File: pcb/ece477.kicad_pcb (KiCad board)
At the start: 2 copper layers, 44 x 40 mm, 21 parts, among them J1 USB_B, SW1 SW_DIP_x01, U1 ESP32-WROOM-32, U2 FT232RL-REEL, U3 LM3671, U4 ADA254, U5 ADA751

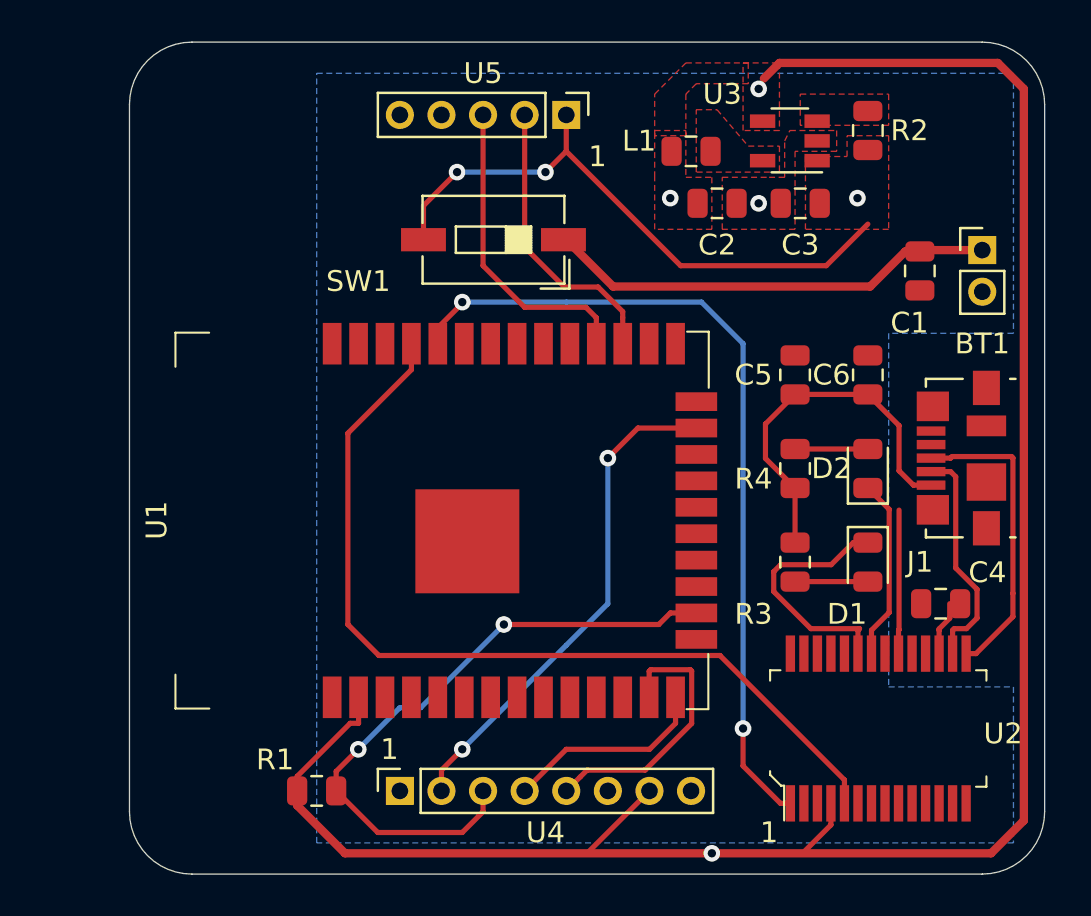
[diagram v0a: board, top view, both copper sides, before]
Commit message: connected to ground plate
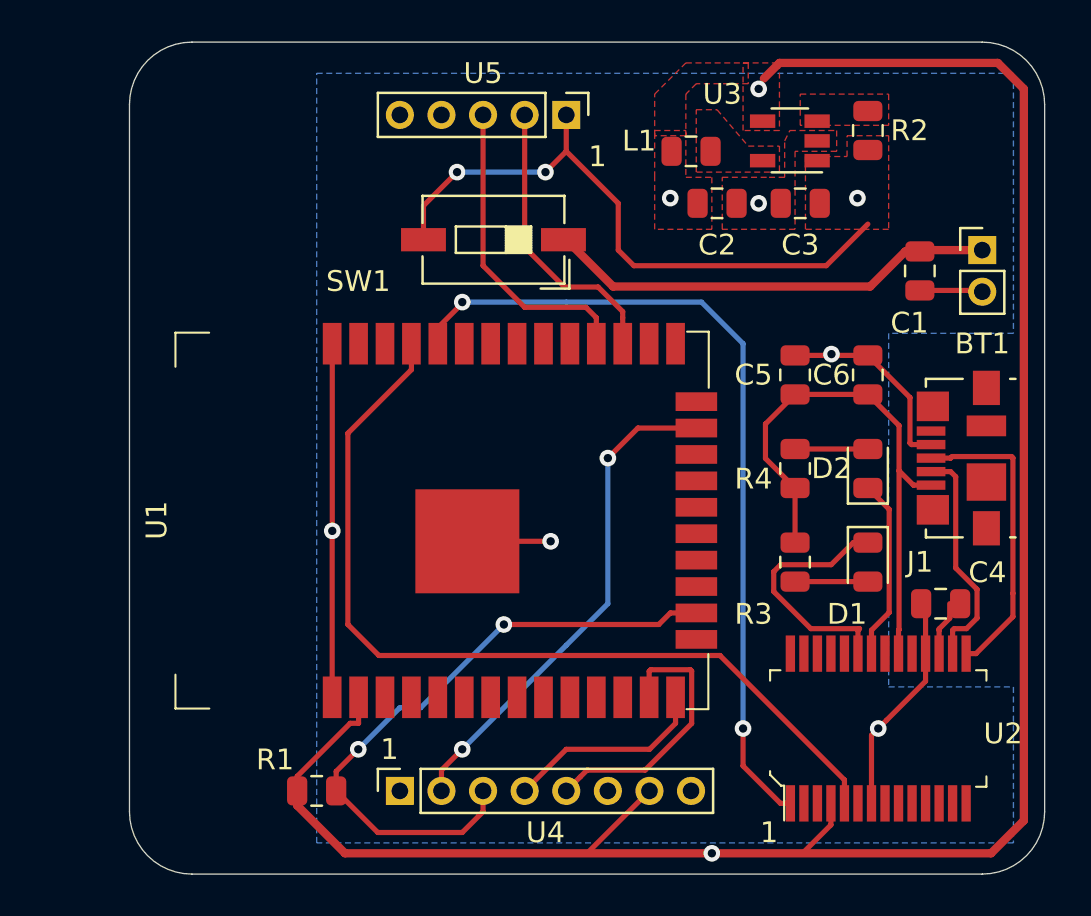
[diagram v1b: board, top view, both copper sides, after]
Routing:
- net GND: track 0.00 -> 44.6 mm, vias 1 -> 5
- net Net-(C5-Pad1): track 24.8 -> 26.7 mm
- net Net-(C3-Pad2): track 28.9 -> 30.3 mm
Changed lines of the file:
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@@
     (thickness 1.6)
     (drawings 16)
-    (tracks 162)
+    (tracks 191)
     (zones 0)
     (modules 21)
@@
   (gr_arc (start 144 78) (end 144 75) (angle -90) (layer Edge.Cuts) (width 0.05))
   (via (at 171.25 82.75) (size 0.8) (drill 0.4) (layers F.Cu B.Cu) (net 1))
+  (via (at 174.75 90) (size 0.8) (drill 0.4) (layers F.Cu B.Cu) (net 1))
+  (segment (start 181.9375 86.9375) (end 182 87) (width 0.25) (layer F.Cu) (net 1))
+  (segment (start 179 86.9375) (end 181.9375 86.9375) (width 0.25) (layer F.Cu) (net 1))
+  (segment (start 174.6875 90.0625) (end 174.75 90) (width 0.25) (layer F.Cu) (net 1))
+  (segment (start 173 90.0625) (end 174.6875 90.0625) (width 0.25) (layer F.Cu) (net 1))
+  (segment (start 174.8125 90.0625) (end 174.75 90) (width 0.25) (layer F.Cu) (net 1))
+  (segment (start 176.5 90.0625) (end 174.8125 90.0625) (width 0.25) (layer F.Cu) (net 1))
+  (segment (start 178.6 94.35) (end 179.54 94.35) (width 0.25) (layer F.Cu) (net 1))
+  (segment (start 178.524999 94.274999) (end 178.6 94.35) (width 0.25) (layer F.Cu) (net 1))
+  (segment (start 178.524999 92.087499) (end 178.524999 94.274999) (width 0.25) (layer F.Cu) (net 1))
+  (segment (start 176.5 90.0625) (end 178.524999 92.087499) (width 0.25) (layer F.Cu) (net 1))
+  (via (at 150.75 98.5) (size 0.8) (drill 0.4) (layers F.Cu B.Cu) (net 1))
+  (segment (start 150.75 89.505) (end 150.745 89.5) (width 0.25) (layer F.Cu) (net 1))
+  (segment (start 150.75 98.5) (end 150.75 89.505) (width 0.25) (layer F.Cu) (net 1))
+  (segment (start 150.745 98.505) (end 150.75 98.5) (width 0.25) (layer F.Cu) (net 1))
+  (segment (start 150.745 106.5) (end 150.745 98.505) (width 0.25) (layer F.Cu) (net 1))
+  (via (at 161.25 99) (size 0.8) (drill 0.4) (layers F.Cu B.Cu) (net 1))
+  (segment (start 161.25 99) (end 157.245 99) (width 0.25) (layer F.Cu) (net 1))
+  (via (at 177 108) (size 0.8) (drill 0.4) (layers F.Cu B.Cu) (net 1))
+  (segment (start 177.399999 107.600001) (end 177 108) (width 0.25) (layer F.Cu) (net 1))
+  (segment (start 177.325 104.675) (end 177.399999 104.749999) (width 0.25) (layer F.Cu) (net 1))
+  (segment (start 176.675 108.325) (end 177 108) (width 0.25) (layer F.Cu) (net 1))
+  (segment (start 176.675 111.6) (end 176.675 108.325) (width 0.25) (layer F.Cu) (net 1))
+  (segment (start 179.275 102.2125) (end 179.275 104.4) (width 0.25) (layer F.Cu) (net 1))
+  (segment (start 179.0625 102) (end 179.275 102.2125) (width 0.25) (layer F.Cu) (net 1))
+  (segment (start 179.275 105.725) (end 177.399999 107.600001) (width 0.25) (layer F.Cu) (net 1))
+  (segment (start 179.275 104.4) (end 179.275 105.725) (width 0.25) (layer F.Cu) (net 1))
   (segment (start 178.3 85.0625) (end 176.6125 86.75) (width 0.4) (layer F.Cu) (net 2))
   (segment (start 179 85.0625) (end 178.3 85.0625) (width 0.4) (layer F.Cu) (net 2))
@@
   (segment (start 162 80.25) (end 162 78.5) (width 0.25) (layer F.Cu) (net 46))
   (via (at 176 82.5) (size 0.8) (drill 0.4) (layers F.Cu B.Cu) (net 46))
-  (segment (start 167.5 85.75) (end 174.5 85.75) (width 0.25) (layer F.Cu) (net 46))
   (segment (start 174.5 85.75) (end 176.5 83.75) (width 0.25) (layer F.Cu) (net 46))
-  (segment (start 162 80.25) (end 167.5 85.75) (width 0.25) (layer F.Cu) (net 46))
+  (segment (start 165.25 85.75) (end 174.5 85.75) (width 0.25) (layer F.Cu) (net 46))
+  (segment (start 164.5 85) (end 165.25 85.75) (width 0.25) (layer F.Cu) (net 46))
+  (segment (start 164.5 82.75) (end 164.5 85) (width 0.25) (layer F.Cu) (net 46))
+  (segment (start 162 80.25) (end 164.5 82.75) (width 0.25) (layer F.Cu) (net 46))
   (segment (start 154 107) (end 152 109) (width 0.25) (layer B.Cu) (net 48))
   (segment (start 152 109) (end 152 109) (width 0.25) (layer B.Cu) (net 48))
@@
   (segment (start 175.8 91.9375) (end 173 91.9375) (width 0.25) (layer F.Cu) (net 57))
   (segment (start 176.5 91.9375) (end 175.8 91.9375) (width 0.25) (layer F.Cu) (net 57))
-  (segment (start 177.975 104.4) (end 177.975 103.275) (width 0.25) (layer F.Cu) (net 57))
-  (segment (start 177.975 103.275) (end 178 103.25) (width 0.25) (layer F.Cu) (net 57))
-  (segment (start 178 103.25) (end 178 97.5) (width 0.25) (layer F.Cu) (net 57))
+  (segment (start 177.975 103.275) (end 177.975 104.4) (width 0.25) (layer F.Cu) (net 57))
+  (segment (start 178 103.25) (end 177.975 103.275) (width 0.25) (layer F.Cu) (net 57))
+  (segment (start 178 95.610002) (end 178 103.25) (width 0.25) (layer F.Cu) (net 57))
   (segment (start 179.925 103.275) (end 179.925 104.4) (width 0.25) (layer F.Cu) (net 58))
   (segment (start 179.925 103.2125) (end 179.925 103.275) (width 0.25) (layer F.Cu) (net 58))

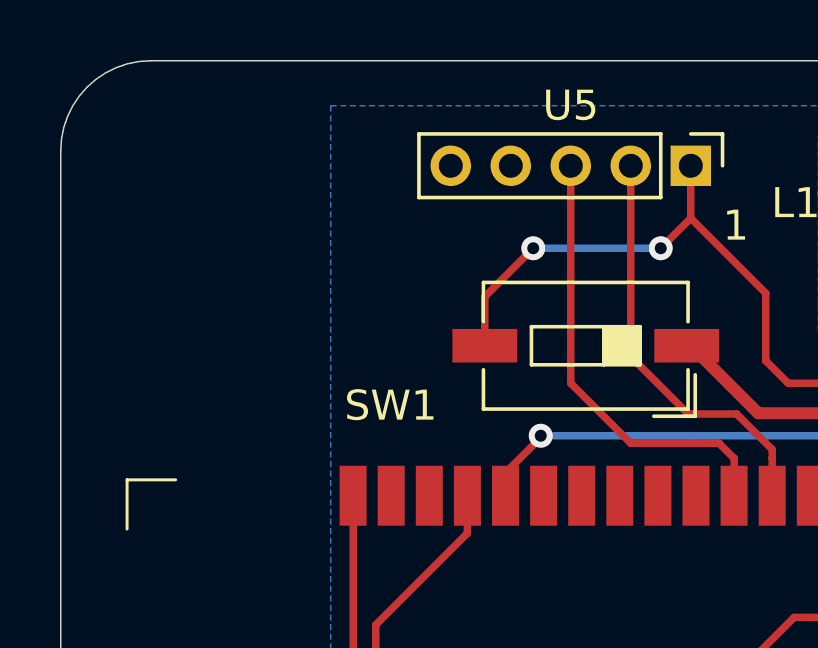
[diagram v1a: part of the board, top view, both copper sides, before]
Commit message: added power LED
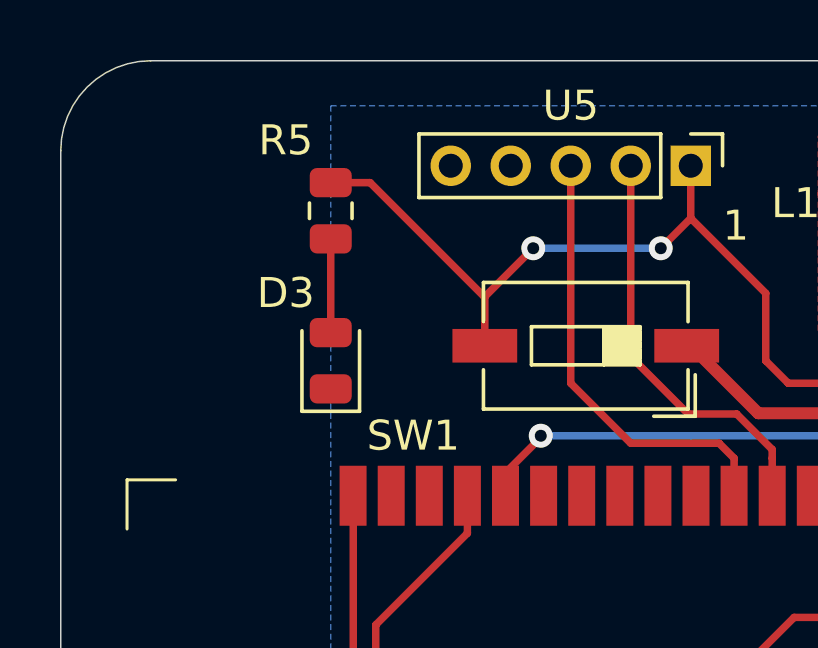
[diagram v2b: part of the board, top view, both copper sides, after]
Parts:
- added D3: LED, LED_SMD:LED_0805_2012Metric, F.Cu at (150.0, 85.0)
- added R5: 1kΩ, Resistor_SMD:R_0805_2012Metric, F.Cu at (150.0, 80.0)
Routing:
- net Net-(C3-Pad2): track 30.3 -> 37.0 mm
- net Net-(D3-Pad2): track 0.00 -> 3.12 mm
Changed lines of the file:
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@@
     (thickness 1.6)
     (drawings 16)
-    (tracks 191)
+    (tracks 195)
     (zones 0)
-    (modules 21)
-    (nets 67)
+    (modules 23)
+    (nets 68)
   )
   (page A4)
@@
   (net 65 "Net-(D2-Pad1)")
   (net 66 "Net-(D2-Pad2)")
+  (net 67 "Net-(D3-Pad2)")
   (net_class Default "This is the default net class."
     (clearance 0.2)
@@
     (add_net "Net-(D2-Pad1)")
     (add_net "Net-(D2-Pad2)")
+    (add_net "Net-(D3-Pad2)")
     (add_net "Net-(J1-Pad2)")
     (add_net "Net-(J1-Pad3)")
@@
     (tags "SMD DIP Switch SPST Slide 6.73mm 264mil SMD LowProfile JPin")
     (attr smd)
-    (fp_text reference SW1 (at 6.5 -2) (layer F.SilkS)
+    (fp_text reference SW1 (at 5.75 -3) (layer F.SilkS)
       (effects (font (size 1 1) (thickness 0.15)))
     )
@@
     (pad 1 smd roundrect (at -0.9375 0 90) (size 0.975 1.4) (layers F.Cu F.Paste F.Mask) (roundrect_rratio 0.25)
       (net 57 "Net-(C5-Pad1)"))
+    (model ${KISYS3DMOD}/Resistor_SMD.3dshapes/R_0805_2012Metric.wrl
+      (at (xyz 0 0 0))
+      (scale (xyz 1 1 1))
+      (rotate (xyz 0 0 0))
+    )
+  )
+  (module LED_SMD:LED_0805_2012Metric (layer F.Cu)
+    (at 150 85 90)
+    (descr "LED SMD 0805 (2012 Metric), square (rectangular) end terminal, IPC_7351 nominal, (Body size source: https://docs.google.com/spreadsheets/d/1BsfQQcO9C6DZCsRaXUlFlo91Tg2WpOkGARC1WS5S8t0/edit?usp=sharing), generated with kicad-footprint-generator")
+    (tags diode)
+    (attr smd)
+    (fp_text reference D3 (at 2.254999 -1.5 180) (layer F.SilkS)
+      (effects (font (size 1 1) (thickness 0.15)))
+    )
+    (fp_text value LED (at 0 1.65 90) (layer F.Fab)
+      (effects (font (size 1 1) (thickness 0.15)))
+    )
+    (fp_line (start 1 -0.6) (end -0.7 -0.6) (layer F.Fab) (width 0.1))
+    (fp_line (start -0.7 -0.6) (end -1 -0.3) (layer F.Fab) (width 0.1))
+    (fp_line (start -1 -0.3) (end -1 0.6) (layer F.Fab) (width 0.1))
+    (fp_line (start -1 0.6) (end 1 0.6) (layer F.Fab) (width 0.1))
+    (fp_line (start 1 0.6) (end 1 -0.6) (layer F.Fab) (width 0.1))
+    (fp_line (start 1 -0.96) (end -1.685 -0.96) (layer F.SilkS) (width 0.12))
+    (fp_line (start -1.685 -0.96) (end -1.685 0.96) (layer F.SilkS) (width 0.12))
+    (fp_line (start -1.685 0.96) (end 1 0.96) (layer F.SilkS) (width 0.12))
+    (fp_line (start -1.68 0.95) (end -1.68 -0.95) (layer F.CrtYd) (width 0.05))
+    (fp_line (start -1.68 -0.95) (end 1.68 -0.95) (layer F.CrtYd) (width 0.05))
+    (fp_line (start 1.68 -0.95) (end 1.68 0.95) (layer F.CrtYd) (width 0.05))
+    (fp_line (start 1.68 0.95) (end -1.68 0.95) (layer F.CrtYd) (width 0.05))
+    (fp_text user %R (at 0 0 90) (layer F.Fab)
+      (effects (font (size 0.5 0.5) (thickness 0.08)))
+    )
+    (pad 1 smd roundrect (at -0.9375 0 90) (size 0.975 1.4) (layers F.Cu F.Paste F.Mask) (roundrect_rratio 0.25)
+      (net 1 GND))
+    (pad 2 smd roundrect (at 0.9375 0 90) (size 0.975 1.4) (layers F.Cu F.Paste F.Mask) (roundrect_rratio 0.25)
+      (net 67 "Net-(D3-Pad2)"))
+    (model ${KISYS3DMOD}/LED_SMD.3dshapes/LED_0805_2012Metric.wrl
+      (at (xyz 0 0 0))
+      (scale (xyz 1 1 1))
+      (rotate (xyz 0 0 0))
+    )
+  )
+  (module Resistor_SMD:R_0805_2012Metric (layer F.Cu)
+    (at 150 80 270)
+    (descr "Resistor SMD 0805 (2012 Metric), square (rectangular) end terminal, IPC_7351 nominal, (Body size source: https://docs.google.com/spreadsheets/d/1BsfQQcO9C6DZCsRaXUlFlo91Tg2WpOkGARC1WS5S8t0/edit?usp=sharing), generated with kicad-footprint-generator")
+    (tags resistor)
+    (attr smd)
+    (fp_text reference R5 (at -2.344999 1.5 180) (layer F.SilkS)
+      (effects (font (size 1 1) (thickness 0.15)))
+    )
+    (fp_text value 1kΩ (at 0 1.65 90) (layer F.Fab)
+      (effects (font (size 1 1) (thickness 0.15)))
+    )
+    (fp_line (start -1 0.6) (end -1 -0.6) (layer F.Fab) (width 0.1))
+    (fp_line (start -1 -0.6) (end 1 -0.6) (layer F.Fab) (width 0.1))
+    (fp_line (start 1 -0.6) (end 1 0.6) (layer F.Fab) (width 0.1))
+    (fp_line (start 1 0.6) (end -1 0.6) (layer F.Fab) (width 0.1))
+    (fp_line (start -0.258578 -0.71) (end 0.258578 -0.71) (layer F.SilkS) (width 0.12))
+    (fp_line (start -0.258578 0.71) (end 0.258578 0.71) (layer F.SilkS) (width 0.12))
+    (fp_line (start -1.68 0.95) (end -1.68 -0.95) (layer F.CrtYd) (width 0.05))
+    (fp_line (start -1.68 -0.95) (end 1.68 -0.95) (layer F.CrtYd) (width 0.05))
+    (fp_line (start 1.68 -0.95) (end 1.68 0.95) (layer F.CrtYd) (width 0.05))
+    (fp_line (start 1.68 0.95) (end -1.68 0.95) (layer F.CrtYd) (width 0.05))
+    (fp_text user %R (at 0 0 90) (layer F.Fab)
+      (effects (font (size 0.5 0.5) (thickness 0.08)))
+    )
+    (pad 1 smd roundrect (at -0.9375 0 270) (size 0.975 1.4) (layers F.Cu F.Paste F.Mask) (roundrect_rratio 0.25)
+      (net 46 "Net-(C3-Pad2)"))
+    (pad 2 smd roundrect (at 0.9375 0 270) (size 0.975 1.4) (layers F.Cu F.Paste F.Mask) (roundrect_rratio 0.25)
+      (net 67 "Net-(D3-Pad2)"))
     (model ${KISYS3DMOD}/Resistor_SMD.3dshapes/R_0805_2012Metric.wrl
       (at (xyz 0 0 0))
@@
   (segment (start 164.5 82.75) (end 164.5 85) (width 0.25) (layer F.Cu) (net 46))
   (segment (start 162 80.25) (end 164.5 82.75) (width 0.25) (layer F.Cu) (net 46))
+  (segment (start 150 79.0625) (end 151.3125 79.0625) (width 0.25) (layer F.Cu) (net 46))
+  (segment (start 155.115 82.865) (end 155.135 82.865) (width 0.25) (layer F.Cu) (net 46))
+  (segment (start 151.3125 79.0625) (end 155.115 82.865) (width 0.25) (layer F.Cu) (net 46))
   (segment (start 154 107) (end 152 109) (width 0.25) (layer B.Cu) (net 48))
   (segment (start 152 109) (end 152 109) (width 0.25) (layer B.Cu) (net 48))
@@
   (segment (start 176.5 96.4375) (end 177.52501 97.46251) (width 0.25) (layer F.Cu) (net 65))
   (segment (start 173 94.5625) (end 176.5 94.5625) (width 0.25) (layer F.Cu) (net 66))
+  (segment (start 150 80.9375) (end 150 84.0625) (width 0.25) (layer F.Cu) (net 67))
   (zone (net 0) (net_name "") (layer F.Cu) (hatch edge 0.508)
     (connect_pads (clearance 0.508))
